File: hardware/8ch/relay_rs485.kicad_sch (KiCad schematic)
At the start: 27 parts, among them J3 RELAY_COM_NO_NC, J4 RS485_A_B_GND_SHIELD, K1 G5LE-1 DC24, Q1 2N7000, U15 ADM2587EBRWZ

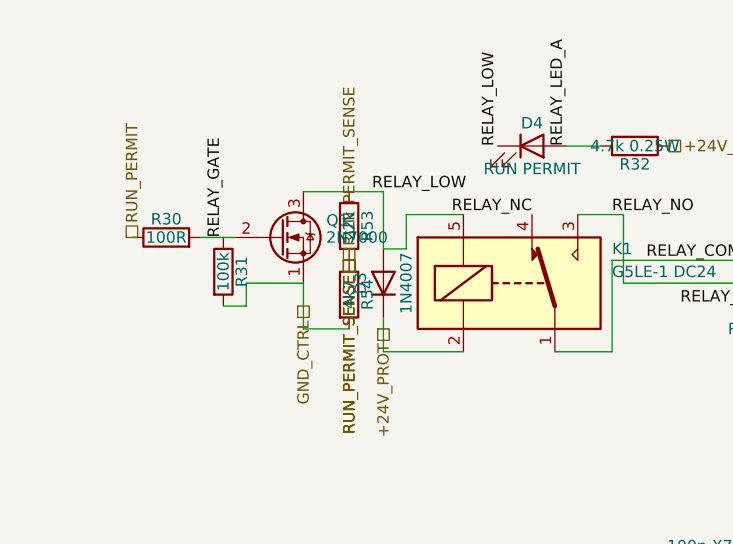
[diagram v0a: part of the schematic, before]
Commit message: REV A2: pre-fabrication fixes I-065..I-069 (decision 0022)
- U10/U11 ISO7760DWR/ISO7761DWR (no F: open input -> HIGH) + R61 2k2 on
  U11 OUTF -> MISO_CTRL so in-circuit ISP works (I-065)
- Q1 BSS131 240 V SOT-23 replaces the 60 V 2N7000 (I-066)
- R53/R54 100k/22k: 0.28 mA into PC2's clamp at 58 V (I-067)
- F1 1812L075/60GR, 60 V 0.75 A 1812 (I-068)
- D2 drawn unidirectional, D3 = M7 SMA, U12 sourcing warning (I-069)
- netlist-baseline-reva2.json (202/163/647), BOARD_REV A2
- board regenerated and re-routed; one hand via for C41.1 (+5V_CTRL)
- run_all.ps1 no longer calls populate_schematic.py (hierarchical sheet)

validate.ps1 2026-09-28 01:07: ERC 0/0, netlist IDENTICAL, DRC 0/0/0/0;
check_board.py all 6 ok; firmware build + 3 suites pass.

Co-Authored-By: Claude Opus 5.5 <noreply@anthropic.com>
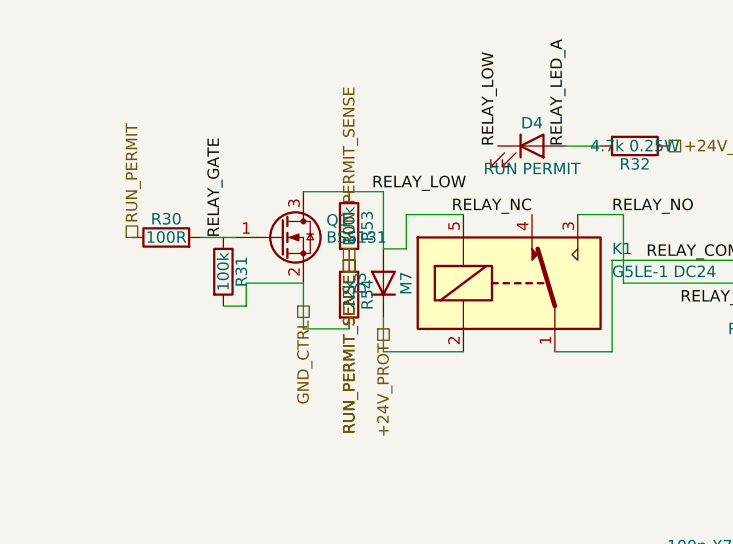
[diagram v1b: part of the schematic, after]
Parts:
- D3: value 1N4007 -> M7; LCSC C727081 -> C95872; MPN 1N4007 -> M7
- Q1: value 2N7000 -> BSS131; footprint Package_TO_SOT_THT:TO-92_Inline_Wide -> Package_TO_SOT_SMD:SOT-23; symbol Transistor_FET:2N7000 -> Transistor_FET:Q_NMOS_GSD; LCSC C9114 -> C151498; MPN 2N7000 -> BSS131H6327XTSA1; Manufacturer onsemi -> Infineon
- R53: value 22k -> 100k; LCSC C17560 -> C149504; MPN 0805W8F2202T5E -> 0805W8F1003T5E
- R54: value 4k7 -> 22k; LCSC C17673 -> C17560; MPN 0805W8F4701T5E -> 0805W8F2202T5E
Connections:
- net GND_CTRL: now also Q1.2 (S); no longer Q1.1 (S)
- net RELAY_GATE: now also Q1.1 (G); no longer Q1.2 (G)
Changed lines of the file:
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@@
 			)
 		)
-		(property "Value" "22k"
+		(property "Value" "100k"
 			(at 106.68 57.15 90)
 			(show_name no)
@@
 			)
 		)
-		(property "Description" "Run-permit read-back divider, upper leg"
+		(property "Description" "Run-permit read-back divider, upper leg (I-067)"
 			(at 106.68 57.15 90)
 			(hide yes)
@@
 			)
 		)
-		(property "MPN" "0805W8F2202T5E"
+		(property "MPN" "0805W8F1003T5E"
 			(at 106.68 57.15 90)
 			(hide yes)
@@
 			)
 		)
-		(property "LCSC" "C17560"
+		(property "LCSC" "C149504"
 			(at 106.68 57.15 90)
 			(hide yes)
@@
 			)
 		)
-		(property "Value" "4k7"
+		(property "Value" "22k"
 			(at 106.68 64.77 90)
 			(show_name no)
@@
 			)
 		)
-		(property "Description" "Run-permit read-back divider, lower leg"
+		(property "Description" "Run-permit read-back divider, lower leg (I-067)"
 			(at 106.68 64.77 90)
 			(hide yes)
@@
 			)
 		)
-		(property "MPN" "0805W8F4701T5E"
+		(property "MPN" "0805W8F2202T5E"
 			(at 106.68 64.77 90)
 			(hide yes)
@@
 			)
 		)
-		(property "LCSC" "C17673"
+		(property "LCSC" "C17560"
 			(at 106.68 64.77 90)
 			(hide yes)
@@
 			)
 		)
-		(property "Value" "1N4007"
+		(property "Value" "M7"
 			(at 113.03 63.5 0)
 			(show_name no)
@@
 			)
 		)
-		(property "Description" "Relay coil flyback clamp"
+		(property "Description" "Relay coil flyback clamp, 1N4007-class in SMA - do not order the through-hole 1N4007 (I-069)"
 			(at 110.49 63.5 0)
 			(hide yes)
@@
 			)
 		)
-		(property "MPN" "1N4007"
+		(property "MPN" "M7"
 			(at 110.49 63.5 0)
 			(hide yes)
@@
 			)
 		)
-		(property "LCSC" "C727081"
+		(property "LCSC" "C95872"
 			(at 110.49 63.5 0)
 			(hide yes)
@@
 	)
 	(symbol
-		(lib_id "Transistor_FET:2N7000")
+		(lib_id "Transistor_FET:Q_NMOS_GSD")
 		(at 99.06 58.42 0)
 		(unit 1)
@@
 			)
 		)
-		(property "Value" "2N7000"
+		(property "Value" "BSS131"
 			(at 104.14 58.42 0)
 			(show_name no)
@@
 			)
 		)
-		(property "Footprint" "Package_TO_SOT_THT:TO-92_Inline_Wide"
+		(property "Footprint" "Package_TO_SOT_SMD:SOT-23"
 			(at 104.14 56.515 0)
 			(hide yes)
@@
 			)
 		)
-		(property "Datasheet" "https://www.vishay.com/docs/70226/70226.pdf"
+		(property "Datasheet" "../../docs/reference/datasheets/BSS131.pdf"
 			(at 104.14 54.61 0)
 			(hide yes)
@@
 			)
 		)
-		(property "Description" "Low-side driver for the 24 V run-permit relay | Manufacturer: onsemi | MPN: 2N7000"
+		(property "Description" "Low-side driver for the 24 V run-permit relay, 240 V: its drain sees the battery rail (I-066) | Manufacturer: Infineon | MPN: BSS131H6327XTSA1"
 			(at 99.06 58.42 0)
 			(hide yes)
@@
 			)
 		)
-		(property "MPN" "2N7000"
+		(property "MPN" "BSS131H6327XTSA1"
 			(at 104.14 54.61 0)
 			(hide yes)
@@
 			)
 		)
-		(property "Manufacturer" "onsemi"
+		(property "Manufacturer" "Infineon"
 			(at 104.14 54.61 0)
 			(hide yes)
@@
 			)
 		)
-		(property "LCSC" "C9114"
+		(property "LCSC" "C151498"
 			(at 104.14 54.61 0)
 			(hide yes)

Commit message: Image guard refuses unapproved images (I-082); refused-ACK reason on LCD (I-088); every BOM line sourced (0027)
- program.ps1 exits 2 on any image but thermo_8ch_max31856.hex (run: legacy image -> exit 2, no avrdude)
- NO ACK CHn HOT/FAULT status after a refused ACK; permit logic unchanged
- LCSC codes: MAX31856MUD+T, LP2985, ADM2587E, ATmega32A-PU, 3296W
- substitutes: K1 G5LE-14 DC24, C53 Rubycon 100YXF22; U12 XP IA0505S from DigiKey
- technician fits THT; 3 boards
build.ps1 exit 0, 3 suites PASS; validate.ps1 01:25 ERC 0/0, IDENTICAL, DRC 0/0/0/0.

Co-Authored-By: Claude Opus 5.5 <noreply@anthropic.com>
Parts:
- K1: value G5LE-1 DC24 -> G5LE-14 DC24; LCSC (none) -> C116965; MPN G5LE-1 DC24 -> G5LE-14 DC24
- U15: LCSC (none) -> C12081; MPN ADM2587EBRWZ -> ADM2587EBRWZ-REEL7
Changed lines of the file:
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@@
 			)
 		)
-		(property "Value" "G5LE-1 DC24"
+		(property "Value" "G5LE-14 DC24"
 			(at 135.89 62.23 0)
 			(show_name no)
@@
 			)
 		)
-		(property "Description" "Energized-to-run SPDT dry-contact output | Manufacturer: Omron Electronics | MPN: G5LE-1 DC24"
+		(property "Description" "Energized-to-run SPDT dry-contact output; G5LE-14 is the fully sealed G5LE-1, same terminals (Omron datasheet) | Manufacturer: Omron Electronics | MPN: G5LE-14 DC24"
 			(at 124.46 63.5 0)
 			(hide yes)
@@
 			)
 		)
-		(property "MPN" "G5LE-1 DC24"
+		(property "MPN" "G5LE-14 DC24"
 			(at 124.46 63.5 0)
 			(hide yes)
@@
 			(show_name no)
 			(do_not_autoplace no)
+			(effects
+				(font
+					(size 1.27 1.27)
+				)
+			)
+		)
+		(property "LCSC" "C116965"
+			(at 124.46 63.5 0)
+			(hide yes)
 			(effects
 				(font
@@
 			)
 		)
-		(property "MPN" "ADM2587EBRWZ"
+		(property "MPN" "ADM2587EBRWZ-REEL7"
 			(at 107.95 116.84 0)
 			(hide yes)
@@
 			(effects
 				(font
+					(size 1.27 1.27)
+				)
+			)
+		)
+		(property "LCSC" "C12081"
+			(at 128.27 116.84 0)
+			(hide yes)
+			(effects
+				(font
